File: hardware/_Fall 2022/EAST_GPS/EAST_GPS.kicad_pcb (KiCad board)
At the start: 2 copper layers, 30.5 x 25.4 mm, 35 parts, among them J1 U.FL, J2 Qwiic Right Angle, J3 PTH, J4 Qwiic Right Angle, U1 Titan X1 GPS

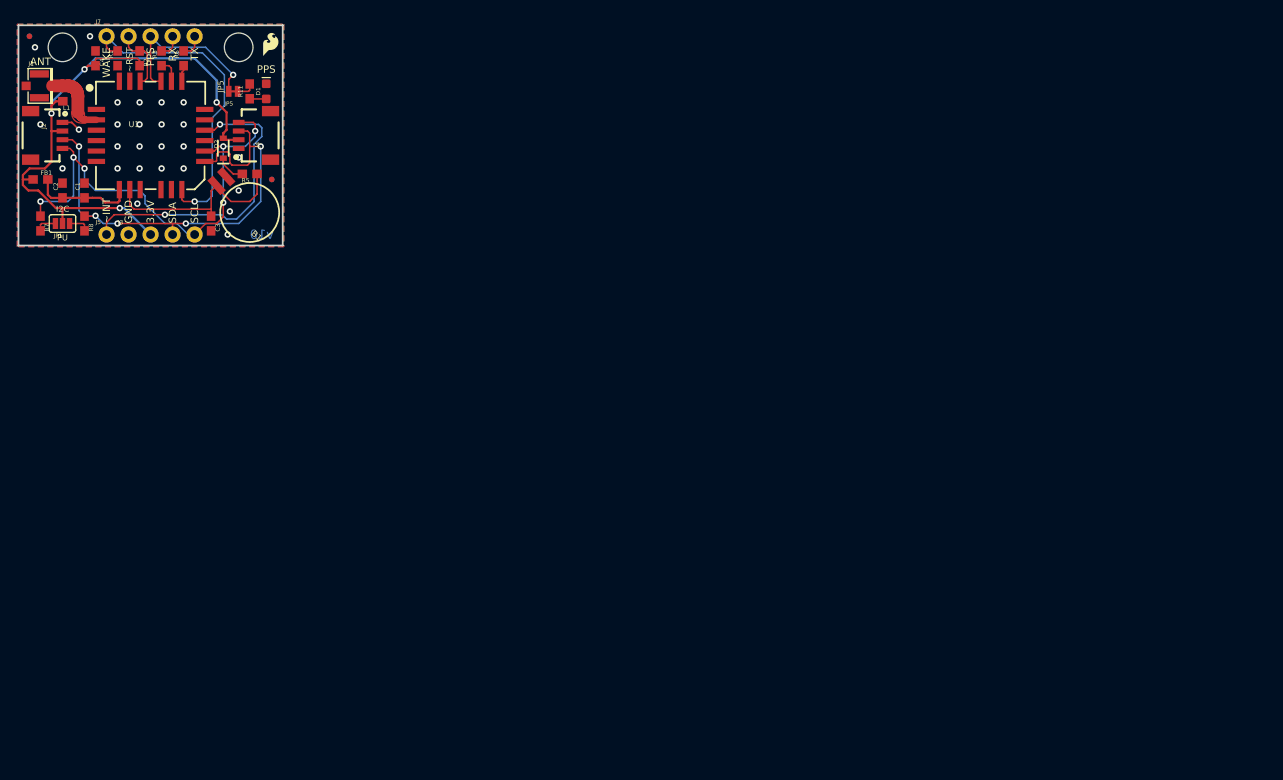
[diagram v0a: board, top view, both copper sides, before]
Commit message: Add east teensy footprint
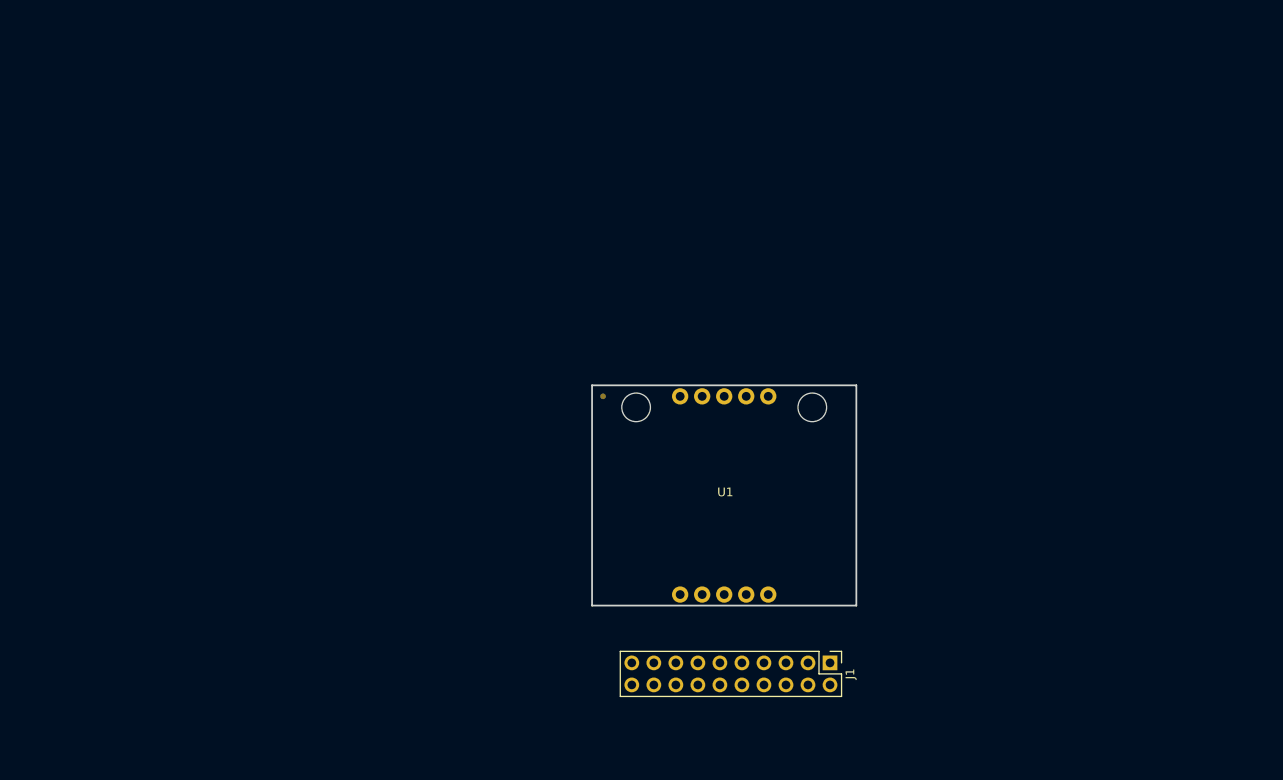
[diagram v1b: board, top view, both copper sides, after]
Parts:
- removed B1: 6.8MM_COIN_CELL, Qwiic GPS - Titan X1 v10:BATTCON-6.8MM
- removed C1: 0.1uF, Qwiic GPS - Titan X1 v10:0603
- removed C2, C3, C4: 1.0uF, Qwiic GPS - Titan X1 v10:0603
- removed D1: BLUE, Qwiic GPS - Titan X1 v10:LED-0603
- removed D2: 0.5A/40V/420mV, Qwiic GPS - Titan X1 v10:SOD-323
- removed FB1: 600Ohm/100MHz, Qwiic GPS - Titan X1 v10:0603
- removed J2, J4: Qwiic Right Angle, Qwiic GPS - Titan X1 v10:1X04_1MM_RA
- removed J3: PTH, Qwiic GPS - Titan X1 v10:1X04_NO_SILK
- removed J5: , Qwiic GPS - Titan X1 v10:1X01_NO_SILK
- removed J7: , Qwiic GPS - Titan X1 v10:1X05_NO_SILK
- removed JP1: , Qwiic GPS - Titan X1 v10:SMT-JUMPER_3_2-NC_PASTE_SILK
- removed JP2, JP6, JP7, JP8: FIDUCIALUFIDUCIAL, Qwiic GPS - Titan X1 v10:MICRO-FIDUCIAL
- removed JP3, JP4: STAND-OFF, Qwiic GPS - Titan X1 v10:STAND-OFF
- removed JP5: , Qwiic GPS - Titan X1 v10:SMT-JUMPER_2_NC_TRACE_NO-SILK
- removed L1: 33nH/±5%/500mA, Qwiic GPS - Titan X1 v10:0603
- removed LOGO1: OSHW-LOGOMINI, Qwiic GPS - Titan X1 v10:OSHW-LOGO-MINI
- removed LOGO2: SFE_LOGO_NAME_FLAME.1_INCH, Qwiic GPS - Titan X1 v10:SFE_LOGO_NAME_FLAME_.1
- removed R1, R2: 10k, Qwiic GPS - Titan X1 v10:0603
- removed R11, R3, R6: 470, Qwiic GPS - Titan X1 v10:0603
- removed R5: 1k, Qwiic GPS - Titan X1 v10:0603
- removed R7, R8: 4.7k, Qwiic GPS - Titan X1 v10:0603
- removed U$2: , Qwiic GPS - Titan X1 v10:SFE_LOGO_FLAME_.1
- J1: value U.FL -> Conn_02x10_Counter_Clockwise; footprint Qwiic GPS - Titan X1 v10:U.FL -> Connector_PinHeader_2.54mm:PinHeader_2x10_P2.54mm_Vertical
- U1: value Titan X1 GPS -> GPS-14414; footprint Qwiic GPS - Titan X1 v10:TITAN_X1_GPS -> GPS_layout:GPS-14414
- moved J1 112.9 mm to (153.0, 118.2), turned to -90 degrees
- moved U1 78.3 mm to (140.9, 99.0)
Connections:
- J1 pad 1: (no net) -> /GND
- J1 pad 2: (no net) -> /3.3V
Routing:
- net (no net): track 353.9 -> 0.00 mm, vias 45 -> 0
- removed copper zone on B.Cu, net (none)
- removed copper zone on F.Cu, net (none)
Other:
- board text removed: "3.3V"
- board text removed: "ANT"
- board text removed: "GND"
- board text removed: "I2C"
- board text removed: "JP5"
- board text removed: "PPS"
- board text removed: "PU"
- board text removed: "Qwiic GPS"
- board text removed: "RX"
- board text removed: "SCL"
- board text removed: "SDA"
- board text removed: "TX"
- board text removed: "WAKE"
- board text removed: "v10"
- board text removed: "~INT"
- board text removed: "~RST"

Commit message: Update east communication and layout
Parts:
- added U2: RFM69HCW_Breakout, Sensors:RFM69HCW_Breakout, F.Cu at (152.4, 94.0)
- J1: value Conn_02x10_Counter_Clockwise -> Conn_02x08_Counter_Clockwise; footprint Connector_PinHeader_2.54mm:PinHeader_2x10_P2.54mm_Vertical -> Connector_PinHeader_2.54mm:PinHeader_2x08_P2.54mm_Vertical
- moved U1 62.2 mm to (188.0, 58.4)
- moved J1 3.38 mm to (149.9, 116.8)
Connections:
- J1 pad 10: /CS 5 -> /RX 2
- J1 pad 11: /TX 3 -> /TX 1
- J1 pad 12: /RX 3 -> /RX 1
- J1 pad 13: /TX 2 -> /SDA 2
- J1 pad 14: /RX 2 -> /SCL 2
- J1 pad 15: /TX 1 -> /SDA 1
- J1 pad 16: /RX 1 -> /SCL 1
- J1 pad 9: /CS 4 -> /TX 2

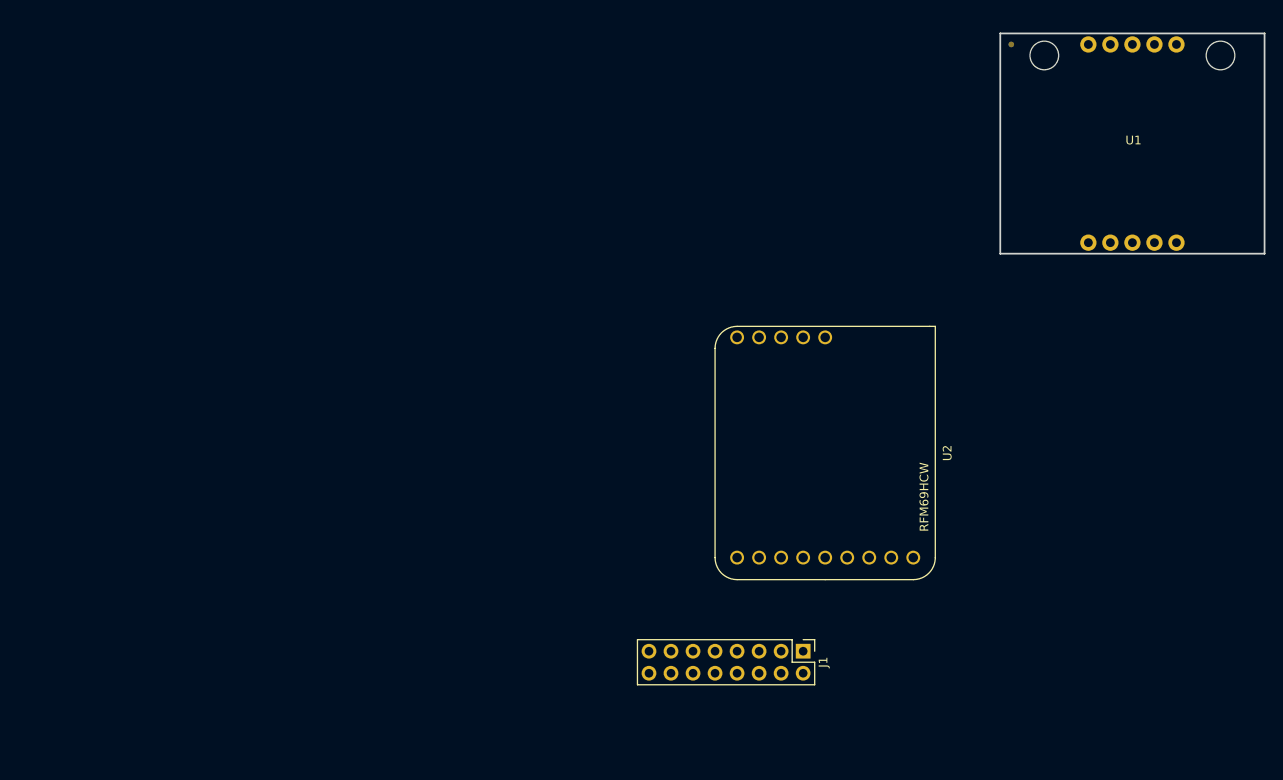
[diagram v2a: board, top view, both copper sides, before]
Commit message: Update pin connections
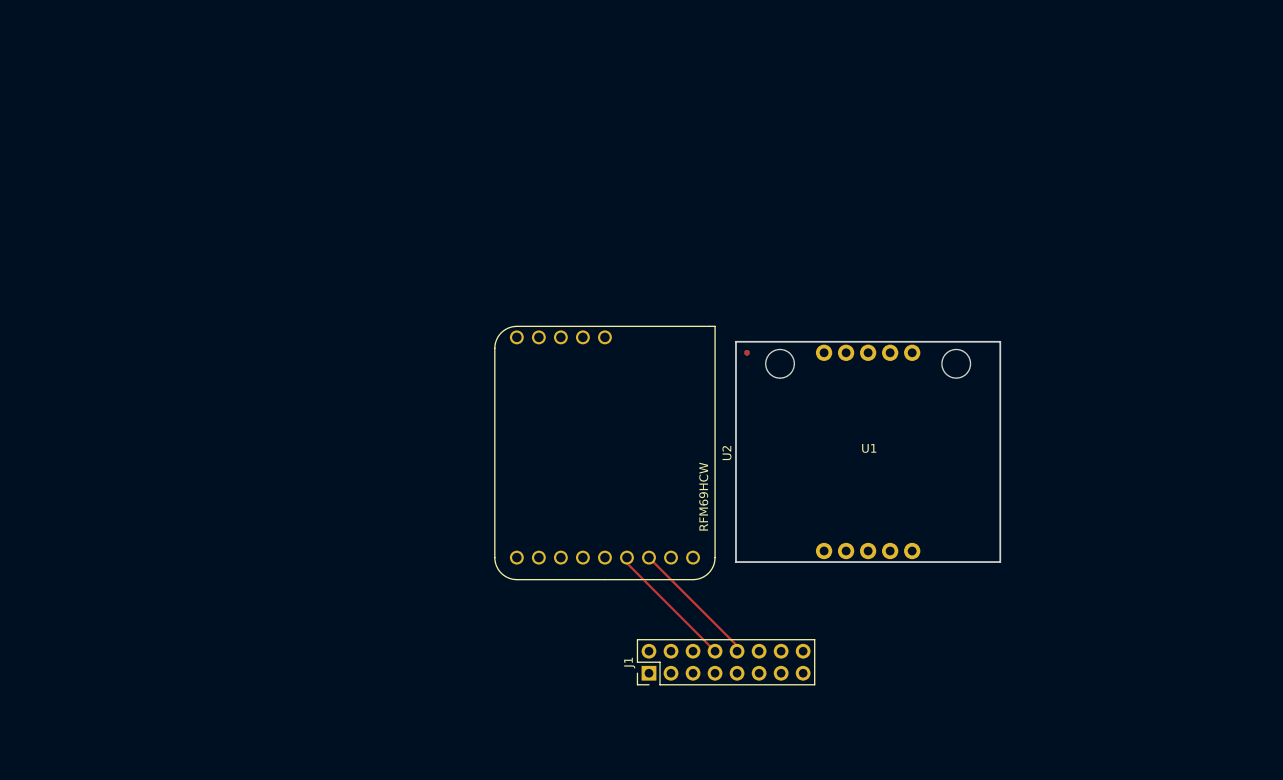
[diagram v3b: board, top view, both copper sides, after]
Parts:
- J1: value Conn_02x08_Counter_Clockwise -> Conn_02x08_Odd_Even
- moved U1 46.8 mm to (157.5, 94.0)
- moved U2 25.4 mm to (127.0, 94.0)
- moved J1 18.0 mm to (132.1, 119.4), turned to 90 degrees
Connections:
- J1 pad 1: /GND -> /RX 2
- J1 pad 10: /RX 2 -> /MISO 1
- J1 pad 12: /RX 1 -> /SCL 2
- J1 pad 13: /SDA 2 -> /RX 1
- J1 pad 14: /SCL 2 -> /SDA 2
- J1 pad 15: /SDA 1 -> /CS 3
- J1 pad 16: /SCL 1 -> /SCK 1
- J1 pad 2: /3.3V -> /GND
- J1 pad 3: /MOSI 1 -> /TX 2
- J1 pad 4: /MISO 1 -> /CS 1
- J1 pad 5: /SCK 1 -> /SCL 1
- J1 pad 6: /CS 1 -> /CS 2
- J1 pad 7: /CS 2 -> /SDA 1
- J1 pad 8: /CS 3 -> /MOSI 1
- J1 pad 9: /TX 2 -> /3.3V
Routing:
- net /MOSI 1: track 0.00 -> 15.0 mm
- net /MISO 1: track 0.00 -> 15.0 mm
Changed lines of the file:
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@@
   (net 24 "unconnected-(U2-Pad14)")
   (footprint "Sensors:RFM69HCW_Breakout" (layer "F.Cu")
-    (at 152.4 93.98 -90)
+    (at 127 93.98 -90)
     (property "Sheetfile" "File: EAST_GPS.kicad_sch")
     (property "Sheetname" "")
@@
   )
   (footprint "GPS_layout:GPS-14414" (layer "F.Cu")
-    (at 187.96 58.42)
+    (at 157.48 93.98)
     (property "Sheetfile" "File: EAST_GPS.kicad_sch")
     (property "Sheetname" "")
@@
   )
   (footprint "Connector_PinHeader_2.54mm:PinHeader_2x08_P2.54mm_Vertical" (layer "F.Cu")
-    (at 149.86 116.84 -90)
+    (at 132.08 119.38 90)
     (descr "Through hole straight pin header, 2x08, 2.54mm pitch, double rows")
     (tags "Through hole pin header THT 2x08 2.54mm double row")
@@
       (effects (font (size 1 1) (thickness 0.15)))
     )
-    (fp_text value "Conn_02x08_Counter_Clockwise" (at 1.27 20.11 90) (layer "F.Fab")
+    (fp_text value "Conn_02x08_Odd_Even" (at 1.27 20.11 90) (layer "F.Fab")
       (effects (font (size 1 1) (thickness 0.15)))
     )
@@
       (effects (font (size 1 1) (thickness 0.15)))
     )
-    (fp_line (start 3.87 -1.33) (end 3.87 19.11) (layer "F.SilkS") (width 0.12))
-    (fp_line (start -1.33 0) (end -1.33 -1.33) (layer "F.SilkS") (width 0.12))
-    (fp_line (start -1.33 1.27) (end -1.33 19.11) (layer "F.SilkS") (width 0.12))
     (fp_line (start -1.33 1.27) (end 1.27 1.27) (layer "F.SilkS") (width 0.12))
     (fp_line (start 1.27 -1.33) (end 3.87 -1.33) (layer "F.SilkS") (width 0.12))
+    (fp_line (start -1.33 1.27) (end -1.33 19.11) (layer "F.SilkS") (width 0.12))
+    (fp_line (start -1.33 19.11) (end 3.87 19.11) (layer "F.SilkS") (width 0.12))
+    (fp_line (start -1.33 0) (end -1.33 -1.33) (layer "F.SilkS") (width 0.12))
     (fp_line (start 1.27 1.27) (end 1.27 -1.33) (layer "F.SilkS") (width 0.12))
+    (fp_line (start 3.87 -1.33) (end 3.87 19.11) (layer "F.SilkS") (width 0.12))
     (fp_line (start -1.33 -1.33) (end 0 -1.33) (layer "F.SilkS") (width 0.12))
-    (fp_line (start -1.33 19.11) (end 3.87 19.11) (layer "F.SilkS") (width 0.12))
+    (fp_line (start -1.8 19.55) (end 4.35 19.55) (layer "F.CrtYd") (width 0.05))
     (fp_line (start 4.35 19.55) (end 4.35 -1.8) (layer "F.CrtYd") (width 0.05))
+    (fp_line (start 4.35 -1.8) (end -1.8 -1.8) (layer "F.CrtYd") (width 0.05))
     (fp_line (start -1.8 -1.8) (end -1.8 19.55) (layer "F.CrtYd") (width 0.05))
-    (fp_line (start -1.8 19.55) (end 4.35 19.55) (layer "F.CrtYd") (width 0.05))
-    (fp_line (start 4.35 -1.8) (end -1.8 -1.8) (layer "F.CrtYd") (width 0.05))
-    (fp_line (start 3.81 -1.27) (end 3.81 19.05) (layer "F.Fab") (width 0.1))
-    (fp_line (start -1.27 19.05) (end -1.27 0) (layer "F.Fab") (width 0.1))
+    (fp_line (start -1.27 0) (end 0 -1.27) (layer "F.Fab") (width 0.1))
     (fp_line (start 0 -1.27) (end 3.81 -1.27) (layer "F.Fab") (width 0.1))
     (fp_line (start 3.81 19.05) (end -1.27 19.05) (layer "F.Fab") (width 0.1))
-    (fp_line (start -1.27 0) (end 0 -1.27) (layer "F.Fab") (width 0.1))
-    (pad "1" thru_hole rect (at 0 0 270) (size 1.7 1.7) (drill 1) (layers *.Cu *.Mask)
-      (net 1 "/GND") (pinfunction "Pin_1") (pintype "passive"))
-    (pad "2" thru_hole oval (at 2.54 0 270) (size 1.7 1.7) (drill 1) (layers *.Cu *.Mask)
-      (net 2 "/3.3V") (pinfunction "Pin_2") (pintype "passive"))
-    (pad "3" thru_hole oval (at 0 2.54 270) (size 1.7 1.7) (drill 1) (layers *.Cu *.Mask)
-      (net 3 "/MOSI 1") (pinfunction "Pin_3") (pintype "passive"))
-    (pad "4" thru_hole oval (at 2.54 2.54 270) (size 1.7 1.7) (drill 1) (layers *.Cu *.Mask)
-      (net 4 "/MISO 1") (pinfunction "Pin_4") (pintype "passive"))
-    (pad "5" thru_hole oval (at 0 5.08 270) (size 1.7 1.7) (drill 1) (layers *.Cu *.Mask)
-      (net 5 "/SCK 1") (pinfunction "Pin_5") (pintype "passive"))
-    (pad "6" thru_hole oval (at 2.54 5.08 270) (size 1.7 1.7) (drill 1) (layers *.Cu *.Mask)
-      (net 6 "/CS 1") (pinfunction "Pin_6") (pintype "passive"))
-    (pad "7" thru_hole oval (at 0 7.62 270) (size 1.7 1.7) (drill 1) (layers *.Cu *.Mask)
-      (net 7 "/CS 2") (pinfunction "Pin_7") (pintype "passive"))
-    (pad "8" thru_hole oval (at 2.54 7.62 270) (size 1.7 1.7) (drill 1) (layers *.Cu *.Mask)
-      (net 8 "/CS 3") (pinfunction "Pin_8") (pintype "passive"))
-    (pad "9" thru_hole oval (at 0 10.16 270) (size 1.7 1.7) (drill 1) (layers *.Cu *.Mask)
-      (net 9 "/TX 2") (pinfunction "Pin_9") (pintype "passive"))
-    (pad "10" thru_hole oval (at 2.54 10.16 270) (size 1.7 1.7) (drill 1) (layers *.Cu *.Mask)
-      (net 10 "/RX 2") (pinfunction "Pin_10") (pintype "passive"))
-    (pad "11" thru_hole oval (at 0 12.7 270) (size 1.7 1.7) (drill 1) (layers *.Cu *.Mask)
+    (fp_line (start -1.27 19.05) (end -1.27 0) (layer "F.Fab") (width 0.1))
+    (fp_line (start 3.81 -1.27) (end 3.81 19.05) (layer "F.Fab") (width 0.1))
+    (pad "1" thru_hole rect (at 0 0 90) (size 1.7 1.7) (drill 1) (layers *.Cu *.Mask)
+      (net 10 "/RX 2") (pinfunction "Pin_1") (pintype "passive"))
+    (pad "2" thru_hole oval (at 2.54 0 90) (size 1.7 1.7) (drill 1) (layers *.Cu *.Mask)
+      (net 1 "/GND") (pinfunction "Pin_2") (pintype "passive"))
+    (pad "3" thru_hole oval (at 0 2.54 90) (size 1.7 1.7) (drill 1) (layers *.Cu *.Mask)
+      (net 9 "/TX 2") (pinfunction "Pin_3") (pintype "passive"))
+    (pad "4" thru_hole oval (at 2.54 2.54 90) (size 1.7 1.7) (drill 1) (layers *.Cu *.Mask)
+      (net 6 "/CS 1") (pinfunction "Pin_4") (pintype "passive"))
+    (pad "5" thru_hole oval (at 0 5.08 90) (size 1.7 1.7) (drill 1) (layers *.Cu *.Mask)
+      (net 16 "/SCL 1") (pinfunction "Pin_5") (pintype "passive"))
+    (pad "6" thru_hole oval (at 2.54 5.08 90) (size 1.7 1.7) (drill 1) (layers *.Cu *.Mask)
+      (net 7 "/CS 2") (pinfunction "Pin_6") (pintype "passive"))
+    (pad "7" thru_hole oval (at 0 7.62 90) (size 1.7 1.7) (drill 1) (layers *.Cu *.Mask)
+      (net 15 "/SDA 1") (pinfunction "Pin_7") (pintype "passive"))
+    (pad "8" thru_hole oval (at 2.54 7.62 90) (size 1.7 1.7) (drill 1) (layers *.Cu *.Mask)
+      (net 3 "/MOSI 1") (pinfunction "Pin_8") (pintype "passive"))
+    (pad "9" thru_hole oval (at 0 10.16 90) (size 1.7 1.7) (drill 1) (layers *.Cu *.Mask)
+      (net 2 "/3.3V") (pinfunction "Pin_9") (pintype "passive"))
+    (pad "10" thru_hole oval (at 2.54 10.16 90) (size 1.7 1.7) (drill 1) (layers *.Cu *.Mask)
+      (net 4 "/MISO 1") (pinfunction "Pin_10") (pintype "passive"))
+    (pad "11" thru_hole oval (at 0 12.7 90) (size 1.7 1.7) (drill 1) (layers *.Cu *.Mask)
       (net 11 "/TX 1") (pinfunction "Pin_11") (pintype "passive"))
-    (pad "12" thru_hole oval (at 2.54 12.7 270) (size 1.7 1.7) (drill 1) (layers *.Cu *.Mask)
-      (net 12 "/RX 1") (pinfunction "Pin_12") (pintype "passive"))
-    (pad "13" thru_hole oval (at 0 15.24 270) (size 1.7 1.7) (drill 1) (layers *.Cu *.Mask)
-      (net 13 "/SDA 2") (pinfunction "Pin_13") (pintype "passive"))
-    (pad "14" thru_hole oval (at 2.54 15.24 270) (size 1.7 1.7) (drill 1) (layers *.Cu *.Mask)
-      (net 14 "/SCL 2") (pinfunction "Pin_14") (pintype "passive"))
-    (pad "15" thru_hole oval (at 0 17.78 270) (size 1.7 1.7) (drill 1) (layers *.Cu *.Mask)
-      (net 15 "/SDA 1") (pinfunction "Pin_15") (pintype "passive"))
-    (pad "16" thru_hole oval (at 2.54 17.78 270) (size 1.7 1.7) (drill 1) (layers *.Cu *.Mask)
-      (net 16 "/SCL 1") (pinfunction "Pin_16") (pintype "passive"))
+    (pad "12" thru_hole oval (at 2.54 12.7 90) (size 1.7 1.7) (drill 1) (layers *.Cu *.Mask)
+      (net 14 "/SCL 2") (pinfunction "Pin_12") (pintype "passive"))
+    (pad "13" thru_hole oval (at 0 15.24 90) (size 1.7 1.7) (drill 1) (layers *.Cu *.Mask)
+      (net 12 "/RX 1") (pinfunction "Pin_13") (pintype "passive"))
+    (pad "14" thru_hole oval (at 2.54 15.24 90) (size 1.7 1.7) (drill 1) (layers *.Cu *.Mask)
+      (net 13 "/SDA 2") (pinfunction "Pin_14") (pintype "passive"))
+    (pad "15" thru_hole oval (at 0 17.78 90) (size 1.7 1.7) (drill 1) (layers *.Cu *.Mask)
+      (net 8 "/CS 3") (pinfunction "Pin_15") (pintype "passive"))
+    (pad "16" thru_hole oval (at 2.54 17.78 90) (size 1.7 1.7) (drill 1) (layers *.Cu *.Mask)
+      (net 5 "/SCK 1") (pinfunction "Pin_16") (pintype "passive"))
     (model "${KICAD6_3DMODEL_DIR}/Connector_PinHeader_2.54mm.3dshapes/PinHeader_2x08_P2.54mm_Vertical.wrl"
       (offset (xyz 0 0 0))
@@
   (gr_line (start 128.8288 116.8654) (end 154.2288 116.8654) (layer "Dwgs.User") (width 0.2))
   (gr_line (start 116.328019 128.2954) (end 166.729581 128.2954) (layer "Dwgs.User") (width 0.2))
+  (segment (start 139.7 116.84) (end 129.54 106.68) (width 0.25) (layer "F.Cu") (net 3))
+  (segment (start 129.54 106.68) (end 129.54 106.045) (width 0.25) (layer "F.Cu") (net 3))
+  (segment (start 142.24 116.205) (end 142.24 116.84) (width 0.25) (layer "F.Cu") (net 4))
+  (segment (start 132.08 106.045) (end 142.24 116.205) (width 0.25) (layer "F.Cu") (net 4))
   (group "" (id 16c30f42-175b-400f-b540-6040af78e635)
     (members
